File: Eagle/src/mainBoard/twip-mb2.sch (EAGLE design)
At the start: 19 parts, among them U1 GY-521MPU6050

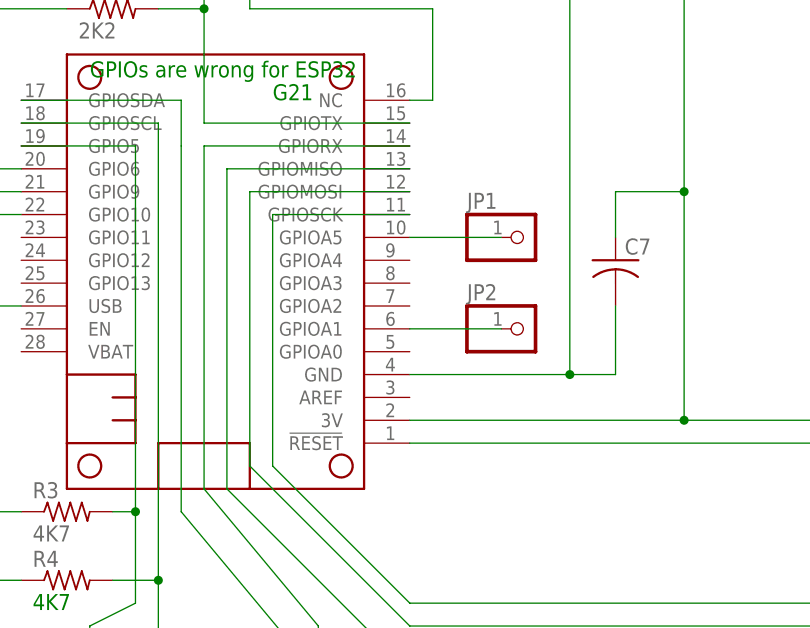
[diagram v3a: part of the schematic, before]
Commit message: Update twip-mb2.sch
 mosfet pullup changes
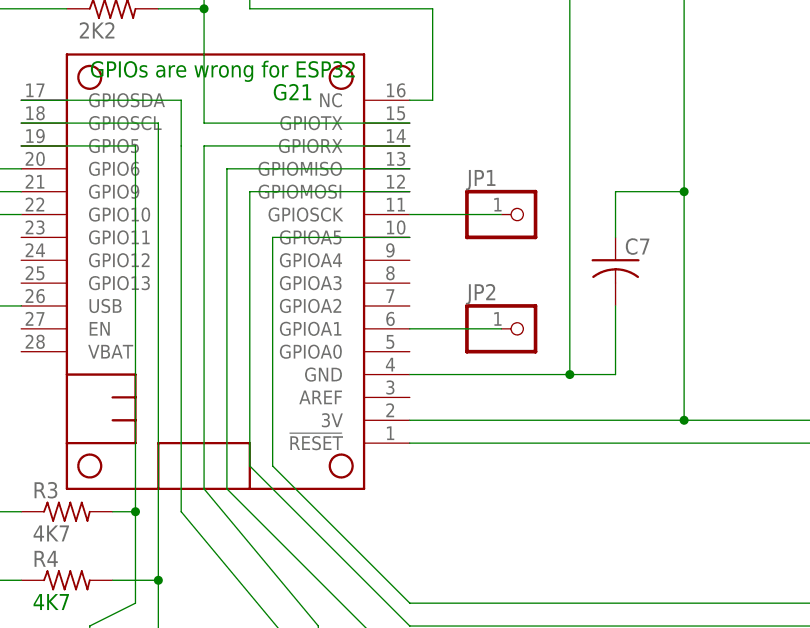
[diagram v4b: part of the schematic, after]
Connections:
- net N$31: now also STEPDRV1.!ENABLE; no longer JP1.1
- net N$32: now also JP1.1; no longer STEPDRV1.!ENABLE
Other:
- moved on the sheet: JP1
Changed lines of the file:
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@@
 <attribute name="VALUE" x="173.736" y="199.009" size="1.778" layer="96"/>
 </instance>
-<instance part="JP1" gate="G$1" x="167.64" y="134.62" smashed="yes">
-<attribute name="NAME" x="161.29" y="137.795" size="1.778" layer="95"/>
-<attribute name="VALUE" x="161.29" y="129.54" size="1.778" layer="96"/>
+<instance part="JP1" gate="G$1" x="167.64" y="137.16" smashed="yes">
+<attribute name="NAME" x="161.29" y="140.335" size="1.778" layer="95"/>
+<attribute name="VALUE" x="161.29" y="132.08" size="1.778" layer="96"/>
 </instance>
 <instance part="JP2" gate="G$1" x="167.64" y="124.46" smashed="yes">
@@
 </segment>
 </net>
-<net name="N$32" class="0">
-<segment>
-<pinref part="STEPDRV1" gate="G$1" pin="!ENABLE"/>
-<wire x1="205.74" y1="15.24" x2="213.36" y2="15.24" width="0.3048" layer="91"/>
-<wire x1="213.36" y1="15.24" x2="213.36" y2="93.98" width="0.3048" layer="91"/>
-<wire x1="213.36" y1="93.98" x2="154.94" y2="93.98" width="0.3048" layer="91"/>
-<wire x1="154.94" y1="93.98" x2="139.7" y2="109.22" width="0.3048" layer="91"/>
-<wire x1="139.7" y1="109.22" x2="139.7" y2="137.16" width="0.3048" layer="91"/>
-<pinref part="MS2" gate="G$1" pin="GPIOSCK"/>
-<wire x1="139.7" y1="137.16" x2="154.94" y2="137.16" width="0.3048" layer="91"/>
-</segment>
-</net>
 <net name="N$34" class="0">
 <segment>
@@
 <segment>
 <pinref part="MS2" gate="G$1" pin="GPIOA5"/>
-<pinref part="JP1" gate="G$1" pin="1"/>
-<wire x1="154.94" y1="134.62" x2="165.1" y2="134.62" width="0.1524" layer="91"/>
+<pinref part="STEPDRV1" gate="G$1" pin="!ENABLE"/>
+<wire x1="205.74" y1="15.24" x2="213.36" y2="15.24" width="0.3048" layer="91"/>
+<wire x1="213.36" y1="15.24" x2="213.36" y2="93.98" width="0.3048" layer="91"/>
+<wire x1="213.36" y1="93.98" x2="154.94" y2="93.98" width="0.3048" layer="91"/>
+<wire x1="154.94" y1="93.98" x2="139.7" y2="109.22" width="0.3048" layer="91"/>
+<wire x1="139.7" y1="109.22" x2="139.7" y2="134.62" width="0.3048" layer="91"/>
+<wire x1="154.94" y1="134.62" x2="139.7" y2="134.62" width="0.1524" layer="91"/>
 </segment>
 </net>
@@
 </segment>
 </net>
+<net name="N$32" class="0">
+<segment>
+<pinref part="MS2" gate="G$1" pin="GPIOSCK"/>
+<pinref part="JP1" gate="G$1" pin="1"/>
+<wire x1="154.94" y1="137.16" x2="165.1" y2="137.16" width="0.1524" layer="91"/>
+</segment>
+</net>

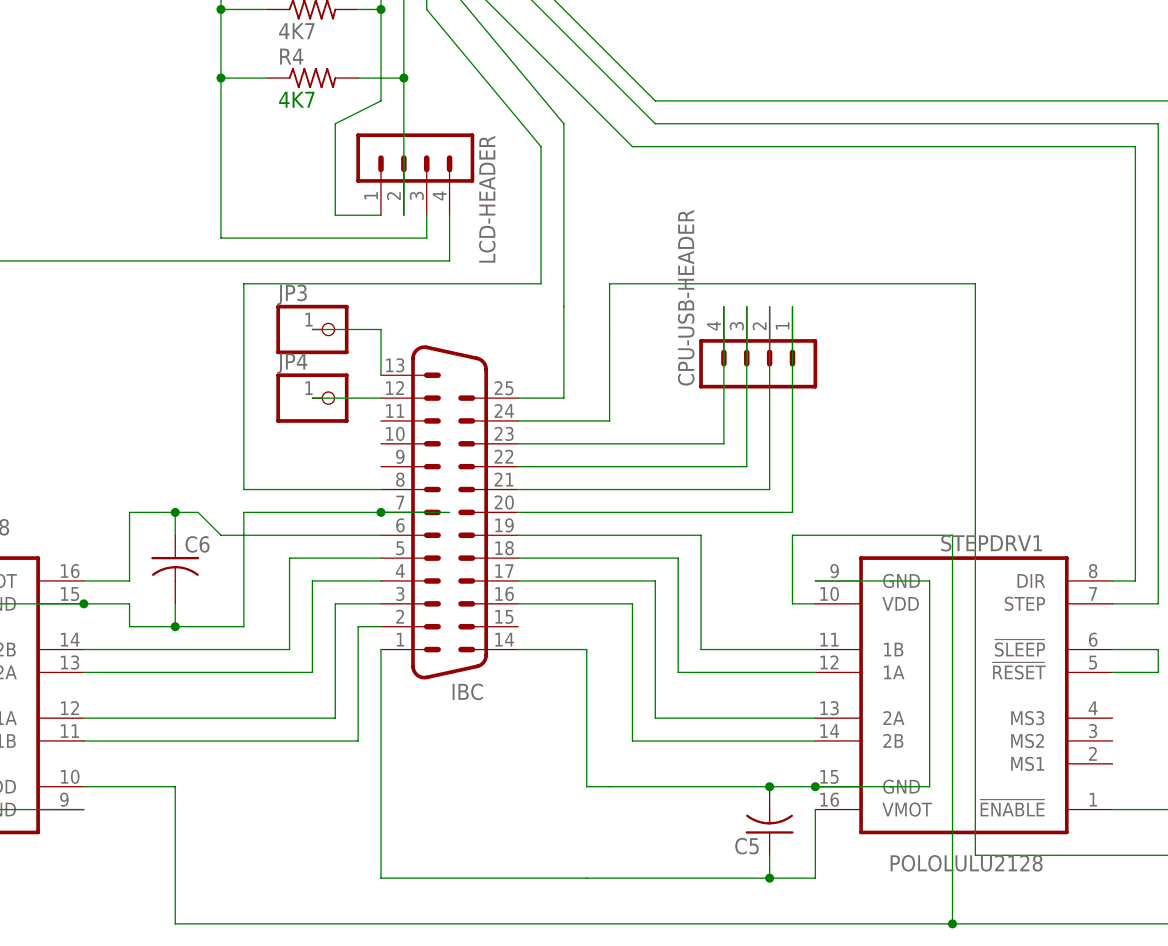
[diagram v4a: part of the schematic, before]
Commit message: Update twip-mb2.sch
big changes to  IBC pinouts  to  shift stepper connectors around
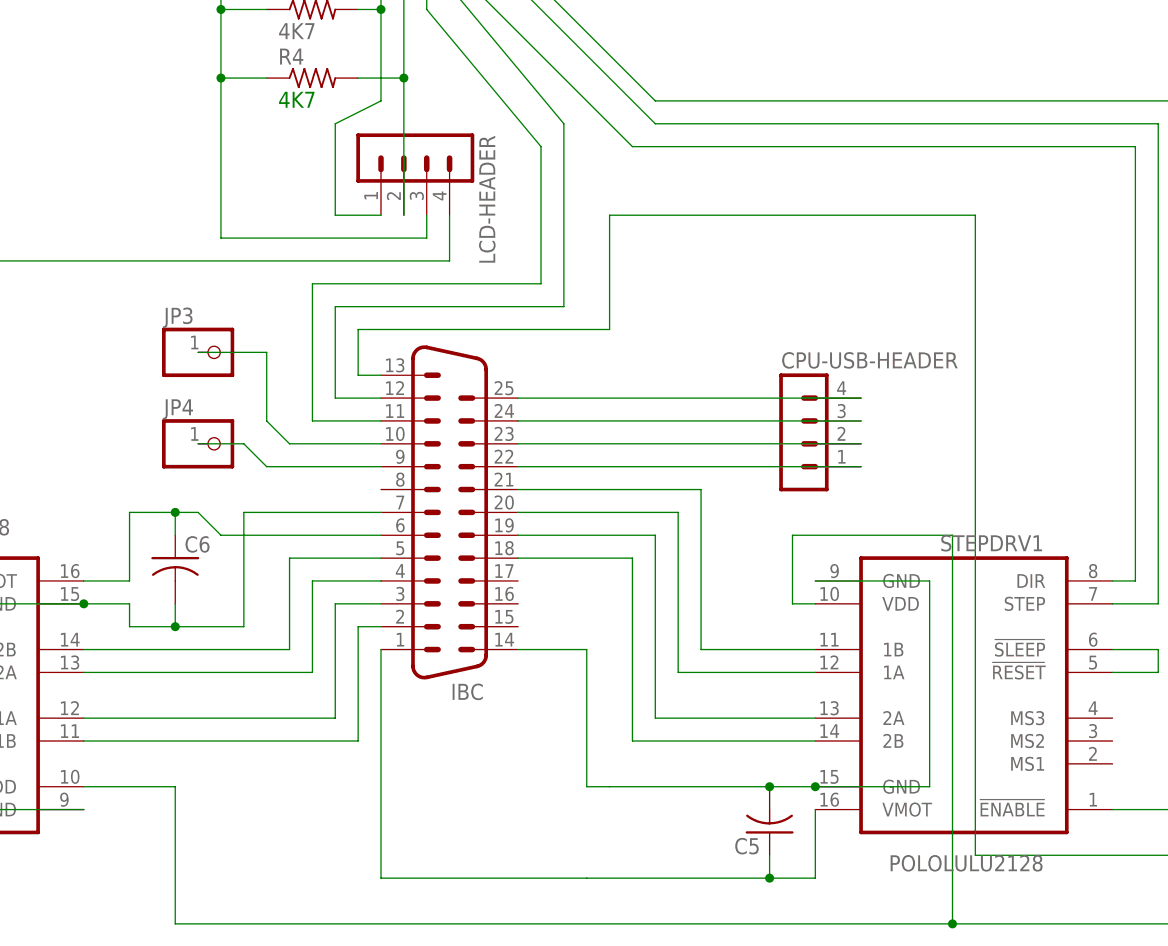
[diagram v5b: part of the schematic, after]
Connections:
- net N$13: now also IBCG$1.25; no longer IBCG$1.23
- net N$14: now also IBCG$1.24; no longer IBCG$1.22
- net N$16: now also IBCG$1.13; no longer IBCG$1.24
- net N$18: now also IBCG$1.23; no longer IBCG$1.21
- net N$19: now also IBCG$1.12; no longer IBCG$1.25
- net N$28: now also IBCG$1.11; no longer IBCG$1.8
- net N$3: now also IBCG$1.18; no longer IBCG$1.16
- net N$30: now also IBCG$1.22; no longer IBCG$1.20
- net N$37: now also IBCG$1.10; no longer IBCG$1.13
- net N$38: now also IBCG$1.9; no longer IBCG$1.12
- net N$4: now also IBCG$1.19; no longer IBCG$1.17
- net N$6: now also IBCG$1.20; no longer IBCG$1.18
- net N$7: now also IBCG$1.21; no longer IBCG$1.19
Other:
- moved on the sheet: CPU-USB-HEADER, JP3, JP4

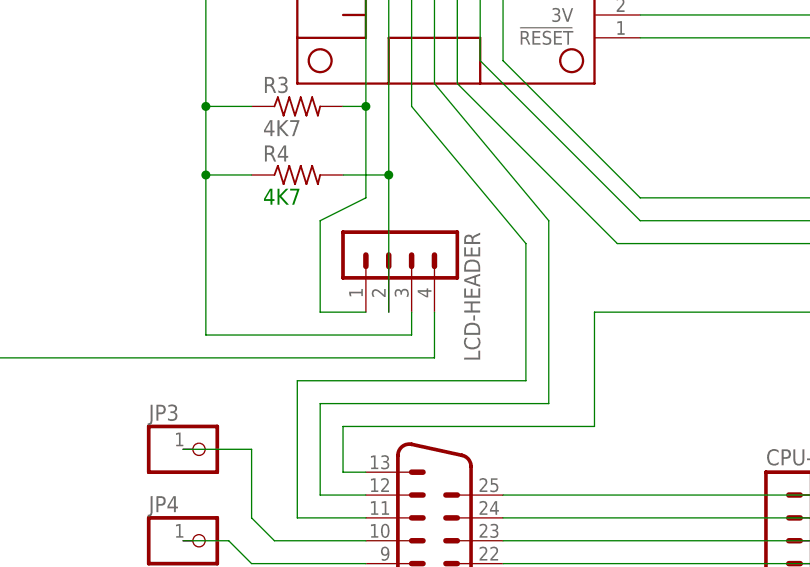
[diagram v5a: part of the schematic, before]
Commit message: Update twip-mb2.sch
change LCD I2C wiring
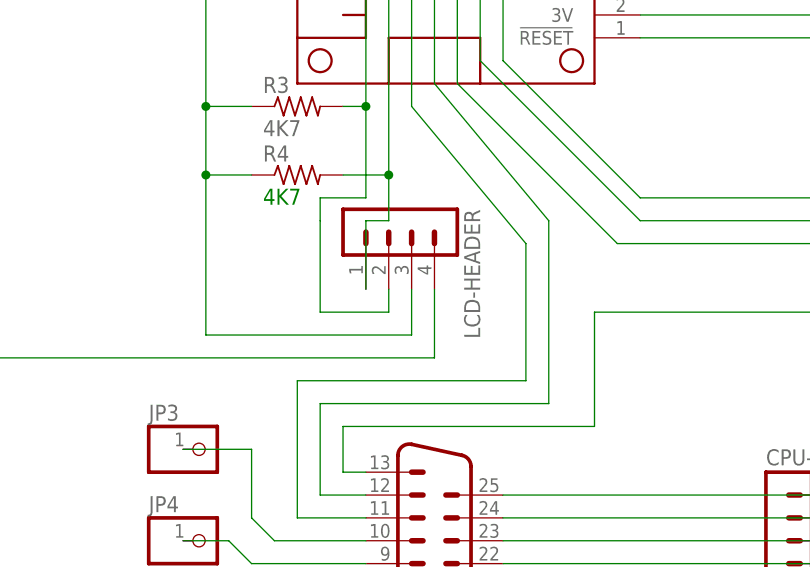
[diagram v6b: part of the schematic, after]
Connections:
- net N$11: now also LCD-HEADER.2; no longer LCD-HEADER.1
- net N$35: now also LCD-HEADER.1; no longer LCD-HEADER.2
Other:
- moved on the sheet: LCD-HEADER
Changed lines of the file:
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@@
 <instances>
 <instance part="U1" gate="G$1" x="132.08" y="193.04" smashed="yes" rot="R270"/>
-<instance part="LCD-HEADER" gate="1" x="129.54" y="88.9" smashed="yes" rot="R270">
-<attribute name="VALUE" x="119.38" y="90.17" size="1.778" layer="96" rot="R270"/>
-<attribute name="NAME" x="135.382" y="90.17" size="1.778" layer="95" rot="R270"/>
+<instance part="LCD-HEADER" gate="1" x="129.54" y="91.44" smashed="yes" rot="R270">
+<attribute name="VALUE" x="119.38" y="92.71" size="1.778" layer="96" rot="R270"/>
+<attribute name="NAME" x="135.382" y="92.71" size="1.778" layer="95" rot="R270"/>
 </instance>
 <instance part="CPU-USB-HEADER" gate="1" x="170.18" y="58.42" smashed="yes">
@@
 <wire x1="111.76" y1="96.52" x2="106.68" y2="96.52" width="0.3048" layer="91"/>
 <junction x="106.68" y="96.52"/>
-<wire x1="129.54" y1="81.28" x2="129.54" y2="78.74" width="0.3048" layer="91"/>
+<wire x1="129.54" y1="83.82" x2="129.54" y2="78.74" width="0.3048" layer="91"/>
 </segment>
 </net>
 <net name="N$11" class="0">
 <segment>
-<pinref part="LCD-HEADER" gate="1" pin="1"/>
-<wire x1="119.38" y1="81.28" x2="124.46" y2="81.28" width="0.3048" layer="91"/>
-<wire x1="124.46" y1="93.98" x2="119.38" y2="91.44" width="0.3048" layer="91"/>
 <wire x1="119.38" y1="91.44" x2="119.38" y2="81.28" width="0.3048" layer="91"/>
 <pinref part="R3" gate="G$1" pin="2"/>
@@
 <pinref part="MS2" gate="G$1" pin="GPIO5"/>
 <wire x1="124.46" y1="144.78" x2="111.76" y2="144.78" width="0.1524" layer="91"/>
+<wire x1="124.46" y1="93.98" x2="119.38" y2="93.98" width="0.1524" layer="91"/>
+<wire x1="119.38" y1="93.98" x2="119.38" y2="91.44" width="0.1524" layer="91"/>
+<wire x1="119.38" y1="81.28" x2="127" y2="81.28" width="0.1524" layer="91"/>
+<pinref part="LCD-HEADER" gate="1" pin="2"/>
+<wire x1="127" y1="81.28" x2="127" y2="83.82" width="0.1524" layer="91"/>
 </segment>
 </net>
@@
 <wire x1="76.2" y1="15.24" x2="91.44" y2="15.24" width="0.3048" layer="91"/>
 <pinref part="LCD-HEADER" gate="1" pin="4"/>
-<wire x1="132.08" y1="81.28" x2="132.08" y2="76.2" width="0.3048" layer="91"/>
+<wire x1="132.08" y1="83.82" x2="132.08" y2="76.2" width="0.3048" layer="91"/>
 <wire x1="101.6" y1="35.56" x2="109.22" y2="35.56" width="0.3048" layer="91"/>
 <junction x="101.6" y="35.56"/>
@@
 <net name="N$35" class="0">
 <segment>
-<pinref part="LCD-HEADER" gate="1" pin="2"/>
 <pinref part="R4" gate="G$1" pin="2"/>
 <wire x1="121.92" y1="96.52" x2="127" y2="96.52" width="0.3048" layer="91"/>
-<wire x1="127" y1="96.52" x2="127" y2="81.28" width="0.3048" layer="91"/>
 <wire x1="127" y1="96.52" x2="127" y2="147.32" width="0.3048" layer="91"/>
-<junction x="127" y="96.52"/>
 <pinref part="MS2" gate="G$1" pin="GPIOSCL"/>
 <wire x1="111.76" y1="147.32" x2="127" y2="147.32" width="0.1524" layer="91"/>
-</segment>
-</net>
+<junction x="127" y="96.52"/>
+<wire x1="127" y1="96.52" x2="127" y2="91.44" width="0.1524" layer="91"/>
+<wire x1="127" y1="91.44" x2="124.46" y2="91.44" width="0.1524" layer="91"/>
+<pinref part="LCD-HEADER" gate="1" pin="1"/>
+<wire x1="124.46" y1="91.44" x2="124.46" y2="83.82" width="0.1524" layer="91"/>
+</segment>
+</net>

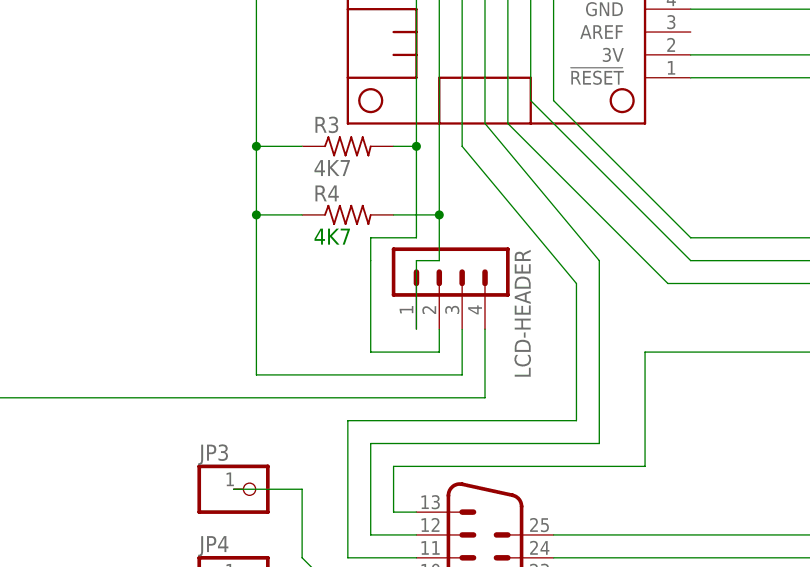
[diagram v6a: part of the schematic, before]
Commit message: Update twip-mb2.sch
change MB2 LCD header wiring to match order of LCD 1602 I2C interface
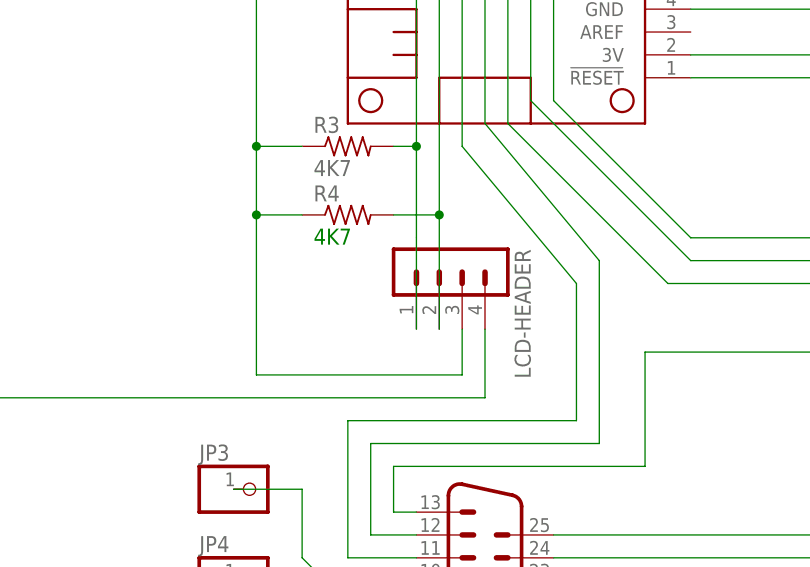
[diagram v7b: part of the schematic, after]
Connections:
- net N$11: now also LCD-HEADER.1; no longer LCD-HEADER.2
- net N$35: now also LCD-HEADER.2; no longer LCD-HEADER.1
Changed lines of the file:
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@@
 <net name="N$11" class="0">
 <segment>
-<wire x1="119.38" y1="91.44" x2="119.38" y2="81.28" width="0.3048" layer="91"/>
 <pinref part="R3" gate="G$1" pin="2"/>
 <wire x1="124.46" y1="144.78" x2="124.46" y2="104.14" width="0.3048" layer="91"/>
@@
 <pinref part="MS2" gate="G$1" pin="GPIO5"/>
 <wire x1="124.46" y1="144.78" x2="111.76" y2="144.78" width="0.1524" layer="91"/>
-<wire x1="124.46" y1="93.98" x2="119.38" y2="93.98" width="0.1524" layer="91"/>
-<wire x1="119.38" y1="93.98" x2="119.38" y2="91.44" width="0.1524" layer="91"/>
-<wire x1="119.38" y1="81.28" x2="127" y2="81.28" width="0.1524" layer="91"/>
-<pinref part="LCD-HEADER" gate="1" pin="2"/>
-<wire x1="127" y1="81.28" x2="127" y2="83.82" width="0.1524" layer="91"/>
+<pinref part="LCD-HEADER" gate="1" pin="1"/>
+<wire x1="124.46" y1="93.98" x2="124.46" y2="83.82" width="0.1524" layer="91"/>
 </segment>
 </net>
@@
 <pinref part="MS2" gate="G$1" pin="GPIOSCL"/>
 <wire x1="111.76" y1="147.32" x2="127" y2="147.32" width="0.1524" layer="91"/>
+<pinref part="LCD-HEADER" gate="1" pin="2"/>
+<wire x1="127" y1="96.52" x2="127" y2="83.82" width="0.1524" layer="91"/>
 <junction x="127" y="96.52"/>
-<wire x1="127" y1="96.52" x2="127" y2="91.44" width="0.1524" layer="91"/>
-<wire x1="127" y1="91.44" x2="124.46" y2="91.44" width="0.1524" layer="91"/>
-<pinref part="LCD-HEADER" gate="1" pin="1"/>
-<wire x1="124.46" y1="91.44" x2="124.46" y2="83.82" width="0.1524" layer="91"/>
 </segment>
 </net>
